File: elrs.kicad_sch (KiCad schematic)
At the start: 83 parts, among them J31 5V, J32 5V, J33 5V, J34 5V, J49 5V, J50 5V, J51 5V, J52 5V, J59 5V, U19 ESP8285H16, U20 SX1281IMLTRT, U24 RFX2401C, U25 RFX2401C, U26 ESP32-PICO-V3, U27 SX1281IMLTRT, U28 SX1281IMLTRT, X1 XTM20026000FT00351005

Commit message: almost finished routing
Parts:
- removed AE2: 47948-0001, lib:ANT-SMD_47948-0001, symbol lib:47948-0001
- removed C2, C83, C84, C85, C86: 1.2p, Capacitor_SMD:C_0402_1005Metric, symbol Device:C
- removed C6, C88, C91, C94, C96: 10nF, Capacitor_SMD:C_0402_1005Metric, symbol Device:C
- removed C76, C77, C87, C90, C93, C95: 100nF, Capacitor_SMD:C_0402_1005Metric, symbol Device:C
- removed C78: 1uF, Capacitor_SMD:C_0402_1005Metric, symbol Device:C
- removed C79, C80, C81, C82: 100n, Capacitor_SMD:C_0402_1005Metric, symbol Device:C
- removed C89, C92: 470nF, Capacitor_SMD:C_0402_1005Metric, symbol Device:C
- removed FL3, FL4: DEA202450BT-3030A1, lib:FILTER-SMD_5P-L2.0-W1.3-L, symbol lib:DEA202450BT-3030A1
- removed J49, J50, J51, J52: 5V, lib:small_pad, symbol Connector_Generic:Conn_01x01
- removed JP3: SolderJumper_2_Open, Jumper:SolderJumper-2_P1.3mm_Open_TrianglePad1.0x1.5mm, symbol Jumper:SolderJumper_2_Open
- removed JP4: U.FL-R-SMT-1(80), lib:RF-SMD_FRF05002-JSS103M, symbol lib:U.FL-R-SMT-1(80)
- removed L1, L12: MGFL2012F150MT-LF (15uH), lib:L0805, symbol lib:MGFL2012F150MT-LF
- removed L10, L11, L6: LQW15AN3N0B00D (3nH), lib:L0402, symbol lib:LQW15AN3N0B00D
- removed L2: ANT8010LL04R2400A, lib:ANT-SMD_L8.0-W1.0-SLDA81-3R010G-S1TF, symbol lib:ANT8010LL04R2400A
- removed LED2: WS2812B-2020, lib:LED-SMD_4P-L2.0-W2.0-TL_WS2812B-2020, symbol lib:WS2812B-2020
- removed OSC2: OW7EL89CENUNFAYLC-52M, lib:OSC-SMD_4P-L2.0-W1.6-BL_TXC_7Z, symbol lib:OW7EL89CENUNFAYLC-52M
- removed R19, R24: 10k, Resistor_SMD:R_0402_1005Metric, symbol Device:R
- removed R20, R21, R22, R23: 100k, Resistor_SMD:R_0402_1005Metric, symbol Device:R
- removed U24, U25: RFX2401C, lib:QFN-16_L3.0-W3.0-P0.50-BL-EP1.7, symbol lib:RFX2401C
- removed U26: ESP32-PICO-V3, lib:LGA-48_L7.0-W7.0-P0.50-BL-EP5.0, symbol lib:ESP32-PICO-V3
- removed U27, U28: SX1281IMLTRT, lib:QFN-24_L4.0-W4.0-P0.50-TL-EP2.6, symbol lib:SX1281IMLTRT
- added R9: 10k, Resistor_SMD:R_0402_1005Metric, symbol Device:R
- C1: value 1.2p -> 10nF; LCSC C327292 -> C15195; now fitted
- C7: LCSC (none) -> C92361
- C9: LCSC (none) -> C15195
- R6, R7, R8: LCSC (none) -> C2909316
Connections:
- net ANT_ESP is gone; now on net GND: C1.1
- net CS: now also R9.1
- net ESP8285_EN: now also R6.2; no longer R8.2
- net GND: now also R9.2; no longer C1.2
- net at C7.1, U20.12 (DCC_FB), U20.2 (VDD_IN): now also C1.2
- net ESP8285_RST renamed ESP_BOOT0
- net ESP_BOOT0: now also R8.2; no longer R6.2
- no-connect marks 47 -> 14

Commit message: Switched to RP2354A and re-routed
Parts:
- removed C10: 100n, Capacitor_SMD:C_0402_1005Metric, symbol Device:C
- removed C15, C20: 1.2p, Capacitor_SMD:C_0402_1005Metric, symbol Device:C
- removed L13: ANT8010LL04R2400A, lib:ANT-SMD_L8.0-W1.0-SLDA81-3R010G-S1TF, symbol lib:ANT8010LL04R2400A
- removed L7, L9: LQW15AN3N0B00D (3nH), lib:L0402, symbol lib:LQW15AN3N0B00D
- removed OSC1: OW7EL89CENUNFAYLC-52M, lib:OSC-SMD_4P-L2.0-W1.6-BL_TXC_7Z, symbol lib:OW7EL89CENUNFAYLC-52M
- added D7: LED, LED_SMD:LED_0603_1608Metric, symbol Device:LED
- added FL1: 2450FM07D0034T, lib:FILTER-SMD_4P-L1.0-W0.5-L, symbol lib:2450FM07D0034T
- added L1: 3n, Inductor_SMD:L_0402_1005Metric, symbol Device:L
- added R33: 3.3k, Resistor_SMD:R_0402_1005Metric, symbol Device:R
- added R35: 10k, Resistor_SMD:R_0402_1005Metric, symbol Device:R
- added X2: Q22FA12800519, lib:CRYSTAL-SMD_4P-L2.0-W1.6-BL, symbol lib:Q22FA12800519
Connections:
- net +3.3V: now also R35.1; no longer U19.14 (GPIO2)
- net GND: now also D7.1 (K), FL1.2 (GND), FL1.4 (GND), X2.2 (GND), X2.4 (GND)
- net RST: now also U19.14 (GPIO2), R35.2; no longer U19.8 (XDP_DCDC)
- net at AE1.3: now also FL1.3 (OUT)
- net at U20.22 (RFIO): now also C14.1, L1.1; no longer C17.1
- net at U20.6 (XTB): now also X2.1
- net ANT_TRACE: now reaches U19.2 (LNA)
- net ANT_TRACE: no longer C14.1
- net RADIO_OSC: no longer names the net of U20.4 (XTA)
- net RADIO_OSC: now also X2.3
- new net: C17.1, FL1.1 (IN), L1.2
- new net: R33.2, U19.8 (XDP_DCDC)
- new net: D7.2 (A), R33.1
- no-connect marks 14 -> 13
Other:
- note added: "On PCB, position pad 1 of filter 0.15mm from RFIO pad on SX1280, lined up with it - per filter DS."
- moved on the sheet: C1, C11, C12, C13, C18, C19, C5, C7, C8, C9, J31, J32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

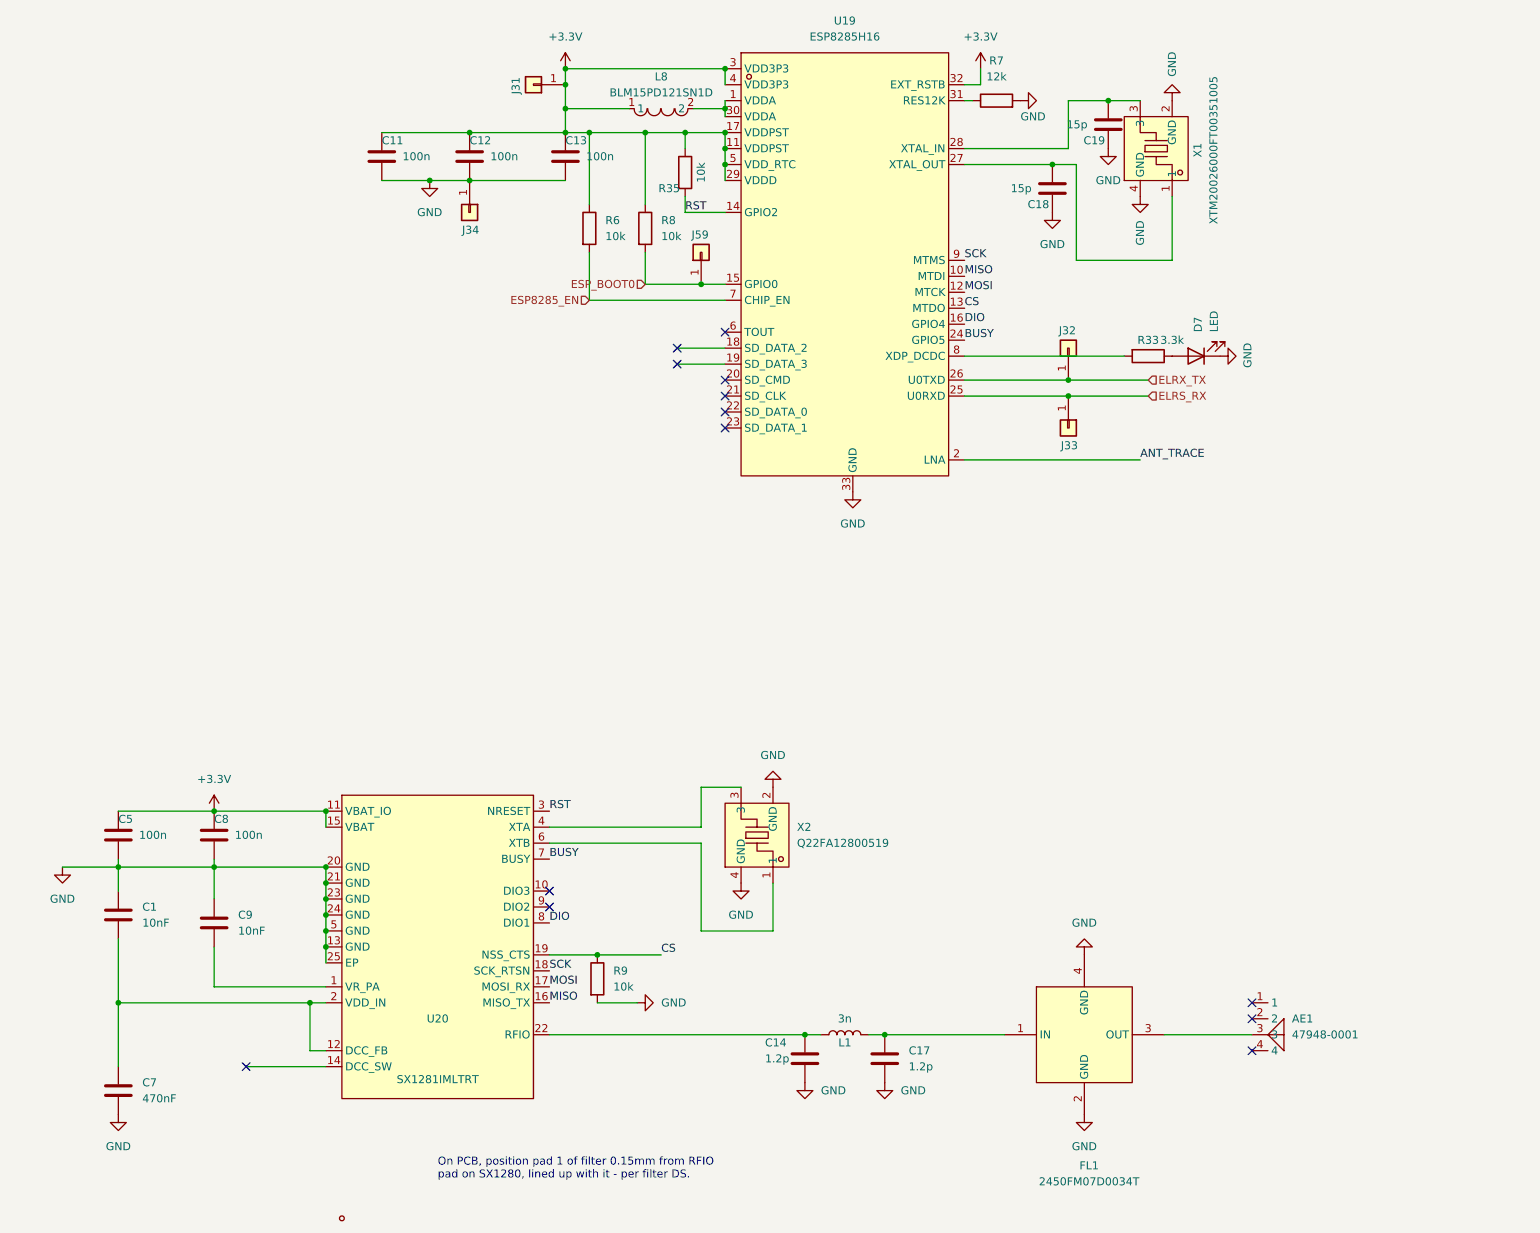
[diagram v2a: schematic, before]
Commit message: Added Open-OSD-X and new layout
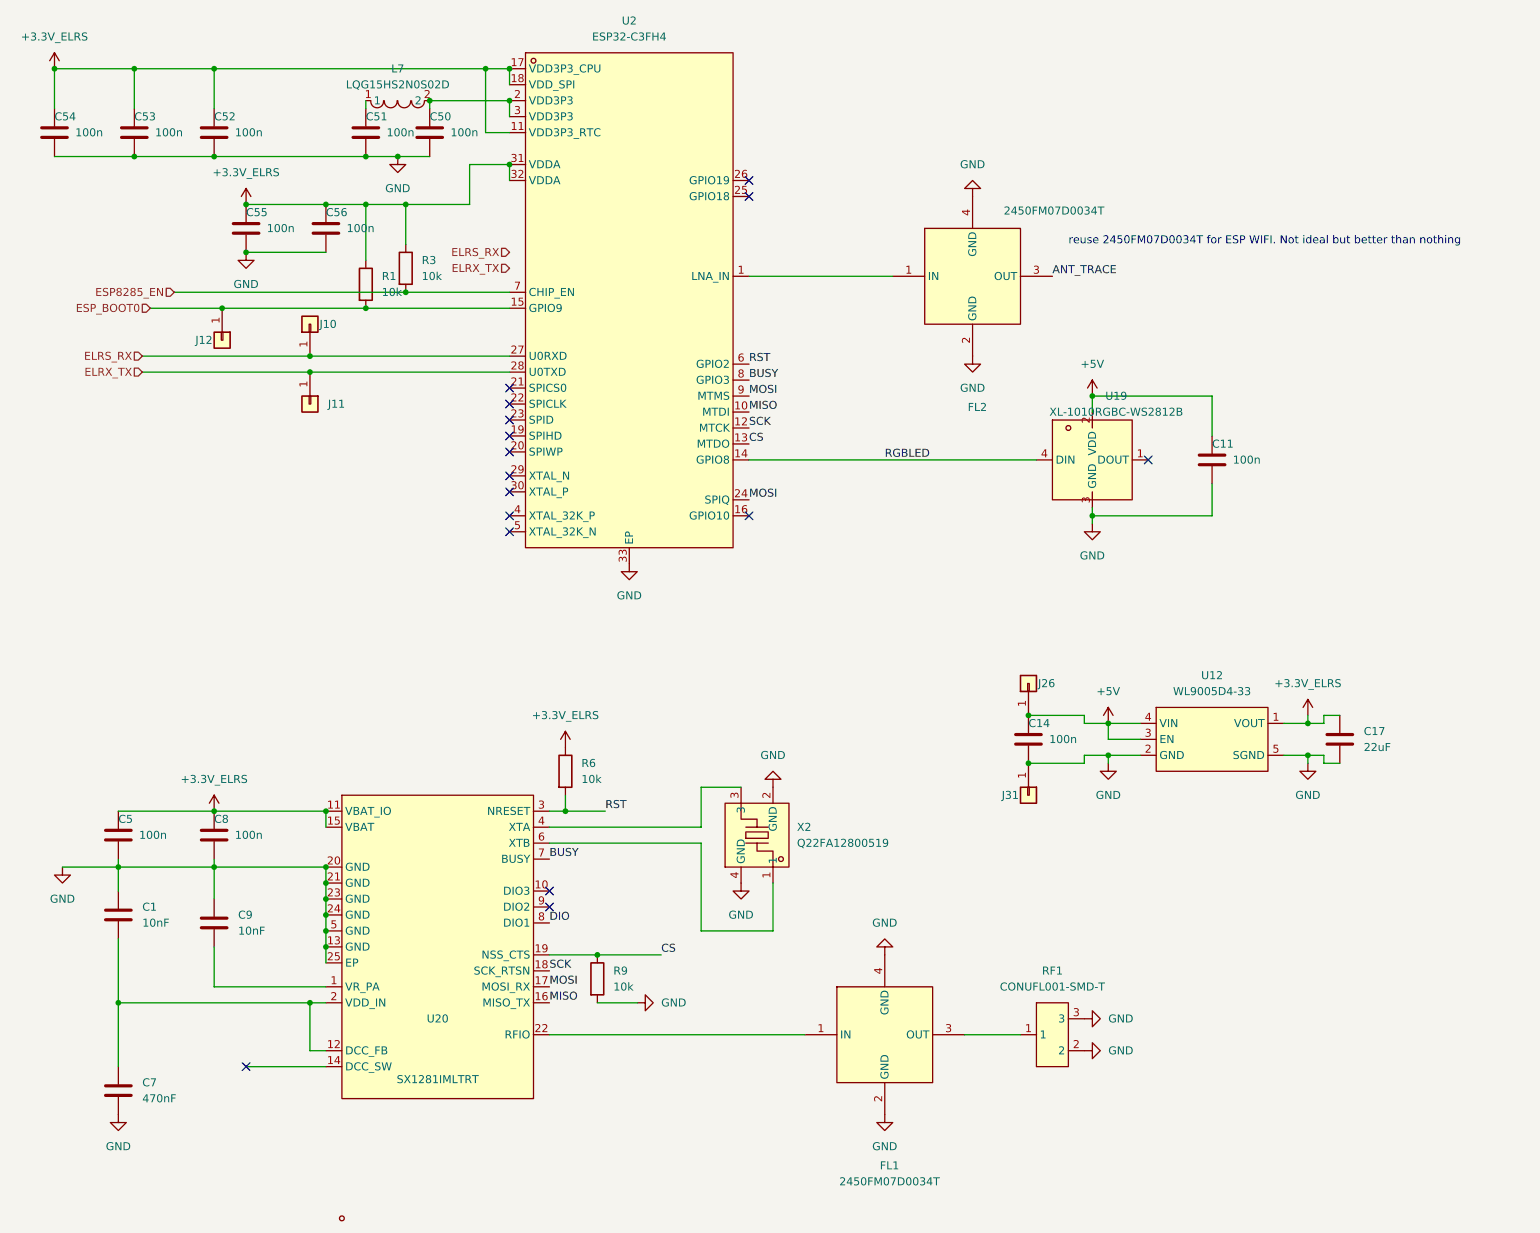
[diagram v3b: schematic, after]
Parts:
- removed AE1: 47948-0001, lib:ANT-SMD_47948-0001, symbol lib:47948-0001
- removed C12, C13: 100n, Capacitor_SMD:C_0402_1005Metric, symbol Device:C
- removed C18, C19: 15p, Capacitor_SMD:C_0402_1005Metric, symbol Device:C
- removed D7: LED, LED_SMD:LED_0603_1608Metric, symbol Device:LED
- removed J32, J33, J34, J59: 5V, lib:small_pad, symbol Connector_Generic:Conn_01x01
- removed L1: 3n, Inductor_SMD:L_0402_1005Metric, symbol Device:L
- removed L8: BLM15PD121SN1D, lib:L0402, symbol lib:BLM15PD121SN1D
- removed R33: 3.3k, Resistor_SMD:R_0402_1005Metric, symbol Device:R
- removed R35, R8: 10k, Resistor_SMD:R_0402_1005Metric, symbol Device:R
- removed R7: 12k, Resistor_SMD:R_0402_1005Metric, symbol Device:R
- removed U19: ESP8285H16, lib:QFN-32_L5.0-W5.0-P0.50-TL-EP3.7, symbol lib:ESP8285H16
- removed X1: XTM20026000FT00351005, lib:CRYSTAL-SMD_4P-L2.0-W1.6-BL, symbol lib:XTM20026000FT00351005
- added C50, C51, C52, C53, C54, C55, C56: 100n, Capacitor_SMD:C_0402_1005Metric, symbol Device:C
- added FL2: 2450FM07D0034T, lib:FILTER-SMD_4P-L1.0-W0.5-L, symbol lib:2450FM07D0034T
- added J10, J11, J12, J26: 5V, lib:small_pad, symbol Connector_Generic:Conn_01x01
- added L7: LQG15HS2N0S02D, lib:L0402, symbol lib:LQG15HS2N0S02D
- added R1, R3: 10k, Resistor_SMD:R_0402_1005Metric, symbol Device:R
- added RF1: CONUFL001-SMD-T, lib:IPEX-SMD_3P-L2.6-W2.6-LS3.0, symbol lib:CONUFL001-SMD-T
- added U12: WL9005D4-33, lib:UDFN-4_L1.0-W1.0-P0.65-TL, symbol lib:WL9005D4-33
- added U19: XL-1010RGBC-WS2812B, lib:LED-SMD_4P-L1.0-W1.0-TL_XL-1010RGBC-WS2812B, symbol lib:XL-1010RGBC-WS2812B
- added U2: ESP32-C3FH4, lib:QFN-32_L5.0-W5.0-P0.50-TL-EP3.7, symbol lib:ESP32-C3FH4
- C14: value 1.2p -> 100n; LCSC C327292 -> C1525
- C17: value 1.2p -> 22uF; LCSC C327292 -> C105226
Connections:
- net ANT_TRACE: now also FL2.3 (OUT)
- net BUSY: now also U2.8 (GPIO3)
- net CS: now also U2.13 (MTDO)
- net ELRS_RX: now also J10.1 (Pin_1), U2.27 (U0RXD)
- net ELRX_TX: now also J11.1 (Pin_1), U2.28 (U0TXD)
- net ESP8285_EN: now also R3.2, U2.7 (CHIP_EN); no longer R6.2
- net ESP_BOOT0: now also J12.1 (Pin_1), R1.2, U2.15 (GPIO9)
- net GND: now also J31.1 (Pin_1), C50.2, C51.2, C52.2, C53.2, C54.2, C55.2, C56.2, FL2.2 (GND), FL2.4 (GND), RF1.2, RF1.3, U12.2 (GND), U12.5 (SGND), U19.3 (GND), U2.33 (EP)
- net MISO: now also U2.10 (MTDI)
- net MOSI: now also U2.24 (SPIQ), U2.9 (MTMS)
- net RST: now also R6.2, U2.6 (GPIO2)
- net SCK: now also U2.12 (MTCK)
- net at U20.22 (RFIO): now also FL1.1 (IN); no longer C14.1
- net +3.3V_ELRS: now reaches C17.1
- net +3.3V_ELRS: now also C5.1, C8.1, R6.1, U20.11 (VBAT_IO), U20.15 (VBAT), C52.1, C53.1, C54.1, C55.1, C56.1, R1.1, R3.1, U12.1 (VOUT), U2.11 (VDD3P3_RTC), U2.17 (VDD3P3_CPU), U2.18 (VDD_SPI), U2.31 (VDDA), U2.32 (VDDA); no longer FL1.1 (IN)
- net at FL1.3 (OUT): now also RF1.1
- removed net +3.3V: C11.1, C5.1, C8.1, J31.1 (Pin_1), R6.1, U20.11 (VBAT_IO), U20.15 (VBAT)
- new net: C51.1, L7.1
- new net: C50.1, L7.2, U2.2 (VDD3P3), U2.3 (VDD3P3)
- new net: FL2.1 (IN), U2.1 (LNA_IN)
- new net +5V: C11.1, C14.1, J26.1 (Pin_1), U12.3 (EN), U12.4 (VIN), U19.2 (VDD)
- new net RGBLED: U19.4 (DIN), U2.14 (GPIO8)
- no-connect marks 13 -> 16
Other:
- note added: "reuse 2450FM07D0034T for ESP WIFI. Not ideal but better than nothing"
- note removed: "On PCB, position pad 1 of filter 0.15mm from RFIO pad on SX1280, lined up with it - per filter DS."
- moved on the sheet: FL1

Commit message: Ordered first revision
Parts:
- removed X2: Q22FA12800519, lib:CRYSTAL-SMD_4P-L2.0-W1.6-BL, symbol lib:Q22FA12800519
- added C59: 15p, Capacitor_SMD:C_0402_1005Metric, symbol Device:C
- added C60: 100n, Capacitor_SMD:C_0402_1005Metric, symbol Device:C
- added OSC1: OW7EL89CENUNFAYLC-52M, lib:OSC-SMD_4P-L2.0-W1.6-BL_TXC_7Z, symbol lib:OW7EL89CENUNFAYLC-52M
- FL1, FL2: value 2450FM07D0034T -> DEA102700LT-6307A2; LCSC Part C2651081 -> C574024
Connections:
- net +3.3V_ELRS: now also C60.1, OSC1.4 (VDD)
- net DIO: now also U2.4 (XTAL_32K_P)
- net GND: now also C59.1, C60.2, OSC1.1 (GND), OSC1.2 (GND)
- net MOSI: no longer U2.24 (SPIQ)
- net at U20.4 (XTA): now also C59.2, OSC1.3 (Out_Put)
- no-connect marks 16 -> 17
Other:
- note added: "reuse DEA102700LT-6307A2for ESP WIFI. Not ideal but better than nothing"
- note removed: "reuse 2450FM07D0034T for ESP WIFI. Not ideal but better than nothing"
